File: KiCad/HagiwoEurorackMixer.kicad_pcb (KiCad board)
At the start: 2 copper layers, 66 x 128.5 mm, 34 parts, among them J1 IN 1, J2 IN 2, J3 IN 3, J4 IN 4, J5 OUT, J6 EURO_PWR_2x5, U2 TL072

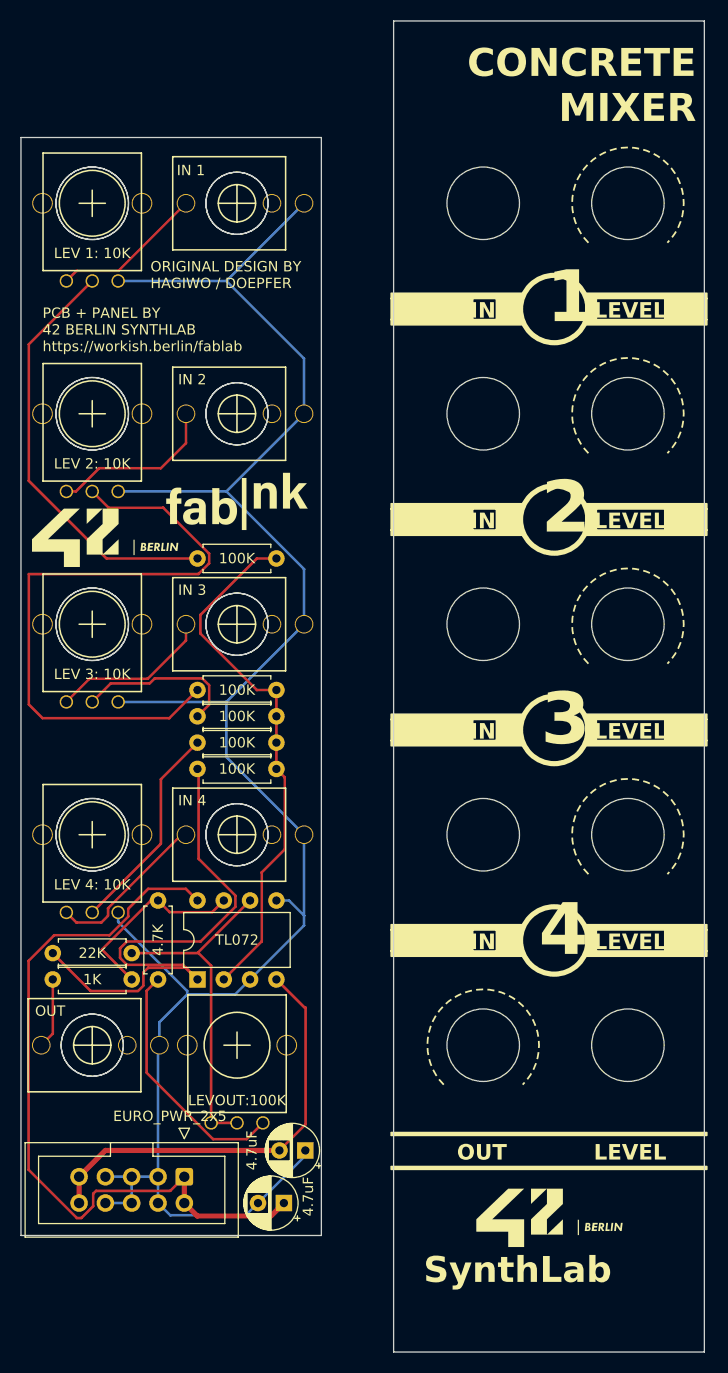
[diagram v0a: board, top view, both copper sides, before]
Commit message: v1.1 complete - fixed power header orientation, implemented ground plane, equal horizontal spacing from board edge for pots and jacks, flipped some components to back and reoriented, rerouted, redesigned panel
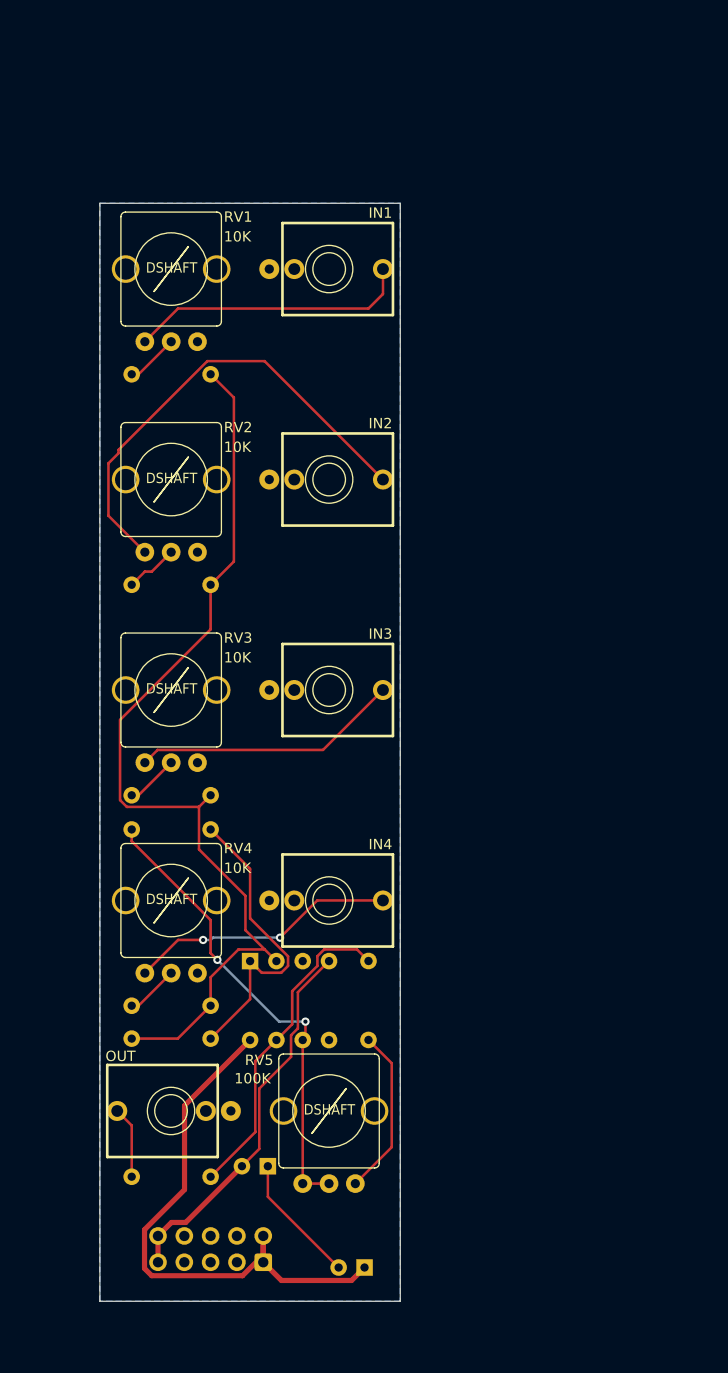
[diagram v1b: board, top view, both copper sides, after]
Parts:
- removed J6: EURO_PWR_2x5, Connector_IDC:IDC-Header_2x05_P2.54mm_Vertical
- removed REF** (x10): MountingHole_6mm, Library:MountingHole_6mm
- removed REF** (x2): Eurorack_Panel_ScrewHole_Oval, Library:Eurorack_Panel_ScrewHole_Oval
- added J7: Eurorack_Power_10pin_Unshrouded, LibraryAll:IDC-Header_2x05_P2.54mm_Vertical_Euro_Power_Striped, B.Cu at (92.4, 155.4)
- C1, C2, R1, R2, R3, R4, R5, R6, R7, R8, U2: moved to B.Cu
- J1: value IN 1 -> IN1; footprint eurocad:PJ301M-12_T_S -> LibraryAll:EighthInch_PJ398SM_T_TN_S
- J2: value IN 2 -> IN2; footprint eurocad:PJ301M-12_T_S -> LibraryAll:EighthInch_PJ398SM_T_TN_S
- J3: value IN 3 -> IN3; footprint eurocad:PJ301M-12_T_S -> LibraryAll:EighthInch_PJ398SM_T_TN_S
- J4: value IN 4 -> IN4; footprint eurocad:PJ301M-12_T_S -> LibraryAll:EighthInch_PJ398SM_T_TN_S
- J5: footprint eurocad:PJ301M-12_T_S -> LibraryAll:EighthInch_PJ398SM_T_TN_S
- RV1: value LEV 1: 10K -> 10K; footprint eurocad:Alpha9mmPot -> LibraryAll:Pot_9mm_DShaft_RemovedPins4_5
- RV2: value LEV 2: 10K -> 10K; footprint eurocad:Alpha9mmPot -> LibraryAll:Pot_9mm_DShaft_RemovedPins4_5
- RV3: value LEV 3: 10K -> 10K; footprint eurocad:Alpha9mmPot -> LibraryAll:Pot_9mm_DShaft_RemovedPins4_5
- RV4: value LEV 4: 10K -> 10K; footprint eurocad:Alpha9mmPot -> LibraryAll:Pot_9mm_DShaft_RemovedPins4_5
- RV5: value LEVOUT:100K -> 100K; footprint eurocad:Alpha9mmPot -> LibraryAll:Pot_9mm_DShaft_RemovedPins4_5
- moved R5 29.5 mm to (79.7, 133.8), turned to 0 degrees
- moved R4 26.2 mm to (79.7, 130.6)
- moved R7 21.1 mm to (102.6, 133.9)
- moved R8 20.5 mm to (87.3, 147.1)
- moved R6 19.4 mm to (87.3, 113.6), turned to 180 degrees
- moved R1 18.9 mm to (79.7, 69.7)
- moved R2 12.0 mm to (79.7, 90.0)
- moved J3 10.9 mm to (98.8, 100.2), turned to 180 degrees
- moved J1 10.9 mm to (98.8, 59.5), turned to 180 degrees
- moved J2 10.9 mm to (98.8, 79.8), turned to 180 degrees
- moved J4 10.9 mm to (98.8, 120.5), turned to 180 degrees
- moved RV5 10.9 mm to (98.8, 140.8), turned to 180 degrees
- moved C1 9.97 mm to (102.2, 155.9)
- moved RV3 9.92 mm to (83.5, 100.2), turned to 180 degrees
- moved RV1 9.92 mm to (83.5, 59.5), turned to 180 degrees
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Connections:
- C1 pad 2: GND -> Net-(C1-Pad2)
- C2 pad 1: GND -> Net-(C1-Pad2)
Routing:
- net GND: track 196.8 -> 0.00 mm
- net Net-(R2-Pad1): track 63.1 -> 5.11 mm
- net Net-(U2A--): track 51.7 -> 92.1 mm
- net Net-(R1-Pad1): track 41.2 -> 5.11 mm
- net Net-(J2-PadT): track 16.3 -> 45.5 mm
- net Net-(R5-Pad2): track 54.5 -> 29.7 mm
- net Net-(U2C-V+): track 72.8 -> 54.3 mm
- net Net-(R4-Pad1): track 20.6 -> 5.11 mm
- net Net-(J1-PadT): track 14.7 -> 27.3 mm
- net Net-(C1-Pad2): track 0.00 -> 12.6 mm
- net Net-(R7-Pad2): track 18.7 -> 31.2 mm
- net Net-(U2B--): track 33.0 -> 45.3 mm, vias 0 -> 2
- net Net-(R3-Pad1): track 16.0 -> 5.11 mm
- net Net-(J3-PadT): track 15.6 -> 25.9 mm
- net Net-(J4-PadT): track 15.9 -> 25.9 mm, vias 0 -> 2
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- added copper zone on B.Cu, net GND
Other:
- board size 66 x 128.5 mm -> 29 x 106 mm
- board text added: "BY 42 BERLIN SYNTHLAB https://github.com/fablabnk/"
- board text added: "CONCRETE MIXER V1.1"
- board text removed: "1"
- board text removed: "2"
- board text removed: "3"
- board text removed: "4"
- board text removed: "CONCRETE MIXER"
- board text removed: "IN"
- board text removed: "LEVEL"
- board text removed: "OUT"
- board text removed: "PCB + PANEL BY 42 BERLIN SYNTHLAB https://workish.berlin/fablab"
- board text removed: "SynthLab"
